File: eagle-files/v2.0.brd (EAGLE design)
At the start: 39.4 x 83.8 mm, 37 parts, among them U2 MLX90614_

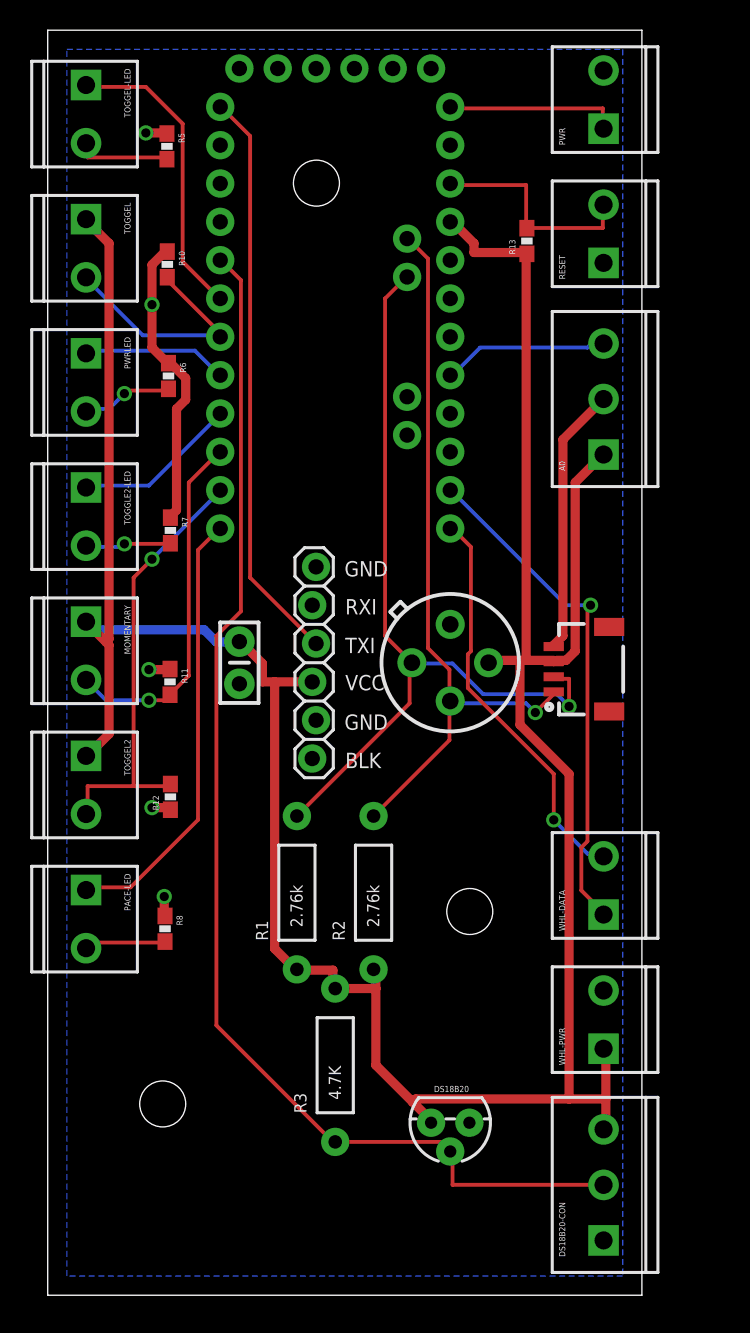
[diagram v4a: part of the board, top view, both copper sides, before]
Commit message: moved parts around on PCB for better smaller fit
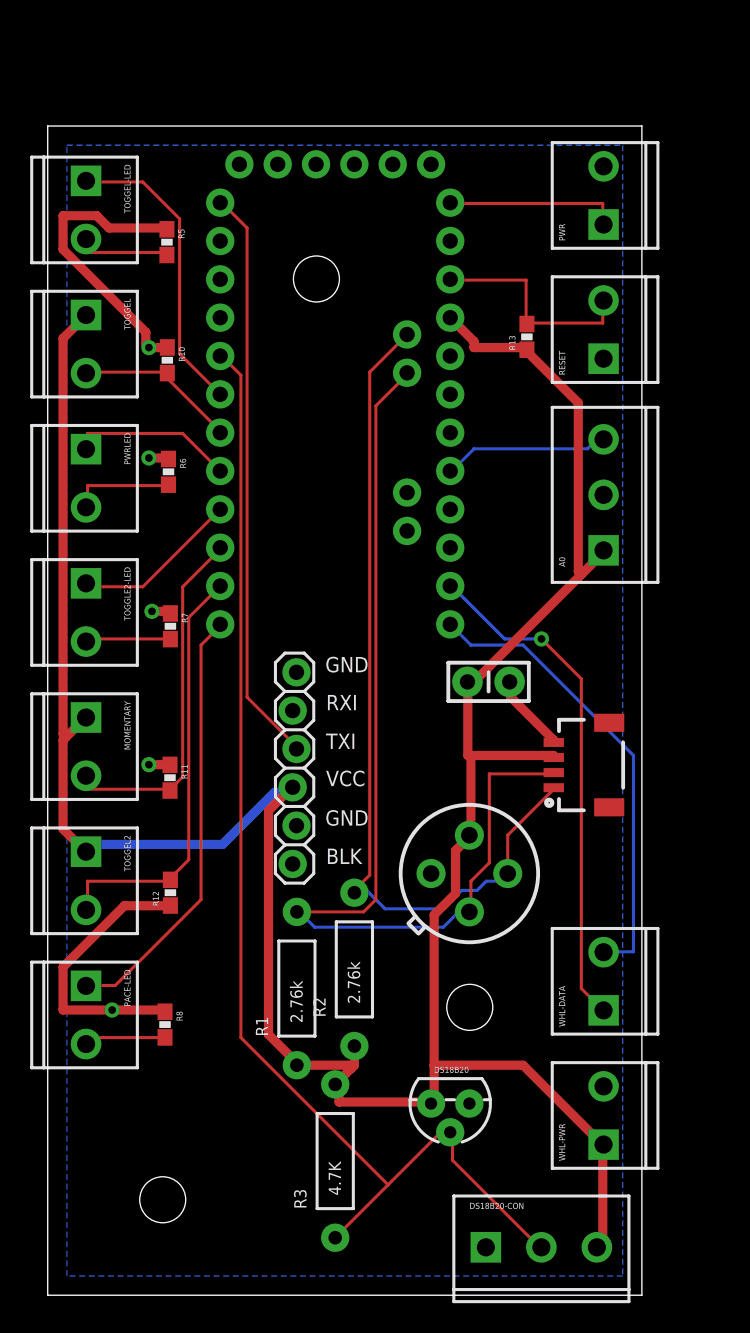
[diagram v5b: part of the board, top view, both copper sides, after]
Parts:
- moved C2 16.6 mm to (29.2, 40.6), turned to 0 degrees
- moved U2 14.0 mm to (27.9, 27.9), turned to 270 degrees
- moved DS18B20-CON 7.65 mm to (29.2, 3.17), turned to 0 degrees
- moved OPENLOG1 7.10 mm to (16.5, 41.3)
- moved PRO_MINI 6.35 mm to (19.1, 59.7)
- moved R5 6.35 mm to (7.90, 69.8)
- moved TOGGEL 6.35 mm to (2.54, 64.8)
- moved TOGGEL-LED 6.35 mm to (2.54, 73.7)
- moved A0 6.35 mm to (36.8, 49.5)
- moved JP6 6.35 mm to (28.0, 19.1)
- moved MLX1 6.35 mm to (33.5, 35.1)
- moved MOMENTARY 6.35 mm to (2.54, 38.1)
- moved PACE-LED 6.35 mm to (2.54, 20.3)
- moved R1 6.35 mm to (16.5, 20.3)
- moved R10 6.35 mm to (7.92, 62.0)
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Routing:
- net 5V: track 196.2 -> 179.2 mm
- net N$9: track 54.9 -> 67.7 mm, vias 1 -> 0
- net N$7: track 49.4 -> 57.2 mm, vias 1 -> 0
- net N$1: track 16.0 -> 10.9 mm
- net GND: track 43.0 -> 47.4 mm
- net N$11: track 26.8 -> 30.7 mm, vias 1 -> 0
- net N$2: track 83.5 -> 80.3 mm
- net N$6: track 9.67 -> 10.9 mm
- net N$18: track 29.5 -> 28.4 mm, vias 1 -> 0
- net N$14: track 6.25 -> 6.91 mm, vias 1 -> 0
- net N$17: track 29.3 -> 28.7 mm
- net N$15: track 5.74 -> 5.70 mm, vias 1 -> 0
- net N$10: vias 1 -> 0
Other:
- board size 39.4 x 83.8 mm -> 39.4 x 77.5 mm

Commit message: added base code for Arduino
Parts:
- renumbered PACE-LED to MOMENTARY-LED
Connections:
- removed net N$7: MLX1.1, PRO_MINI.A5, R2.P$2, U2.2
- removed net N$9: MLX1.2, PRO_MINI.A4, R1.P$2, U2.1
- new net N$21: MLX1.2, PRO_MINI.A5, R2.P$2, U2.2
- new net N$22: MLX1.1, PRO_MINI.A4, R1.P$2, U2.1
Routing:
- net N$9: track 67.7 -> 0.00 mm
- net N$22: track 0.00 -> 65.3 mm
- net N$21: track 0.00 -> 60.0 mm
- net N$7: track 57.2 -> 0.00 mm
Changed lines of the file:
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@@
 <element name="WHL-PWR" library="SparkFun-Connectors" package="SCREWTERMINAL-3.5MM-2_LOCK" value="" x="36.83" y="10.16" rot="R90"/>
 <element name="WHL-DATA" library="SparkFun-Connectors" package="SCREWTERMINAL-3.5MM-2_LOCK" value="" x="36.83" y="19.05" rot="R90"/>
-<element name="PACE-LED" library="SparkFun-Connectors" package="SCREWTERMINAL-3.5MM-2_LOCK" value="" x="2.54" y="20.32" rot="R270"/>
+<element name="MOMENTARY-LED" library="SparkFun-Connectors" package="SCREWTERMINAL-3.5MM-2_LOCK" value="" x="2.54" y="20.32" rot="R270"/>
 <element name="R8" library="SparkFun-Resistors" package="0603-RES" value="330" x="7.7724" y="17.9324" rot="R270">
 <attribute name="PROD_ID" value="RES-00818" x="7.7724" y="17.9324" size="1.778" layer="27" rot="R270" display="off"/>
@@
 <via x="6.7056" y="62.7888" extent="1-16" drill="0.508"/>
 <via x="4.2672" y="18.8976" extent="1-16" drill="0.508"/>
-<wire x1="36.83" y1="53.03" x2="36.83" y2="62.0522" width="0" layer="19" extent="1-1"/>
+<wire x1="36.83" y1="62.0522" x2="36.83" y2="53.03" width="0" layer="19" extent="1-1"/>
 </signal>
 <signal name="N$4">
@@
 <wire x1="16.4592" y1="36.3728" x2="16.4846" y2="36.195" width="0.2032" layer="1"/>
 <wire x1="11.5824" y1="72.3392" x2="11.43" y2="72.39" width="0.2032" layer="1"/>
-</signal>
-<signal name="N$7">
-<contactref element="MLX1" pad="1"/>
-<contactref element="U2" pad="2"/>
-<contactref element="PRO_MINI" pad="A5"/>
-<contactref element="R2" pad="P$2"/>
-<wire x1="30.48" y1="30.48" x2="33.528" y2="33.528" width="0.2032" layer="1"/>
-<wire x1="30.48" y1="27.94" x2="30.48" y2="30.48" width="0.2032" layer="1"/>
-<wire x1="33.528" y1="33.528" x2="33.528" y2="33.6282" width="0.2032" layer="1"/>
-<wire x1="21.336" y1="27.8384" x2="20.32" y2="26.8224" width="0.2032" layer="1"/>
-<wire x1="21.336" y1="61.1632" x2="21.336" y2="27.8384" width="0.2032" layer="1"/>
-<wire x1="23.7744" y1="63.6016" x2="21.336" y2="61.1632" width="0.2032" layer="1"/>
-<wire x1="20.32" y1="26.8224" x2="20.32" y2="26.67" width="0.2032" layer="1"/>
-<wire x1="23.7744" y1="63.6016" x2="23.8125" y2="63.65875" width="0.2032" layer="1"/>
-<wire x1="30.0736" y1="27.432" x2="30.48" y2="27.8384" width="0.2032" layer="16"/>
-<wire x1="29.0576" y1="27.432" x2="30.0736" y2="27.432" width="0.2032" layer="16"/>
-<wire x1="28.448" y1="26.8224" x2="29.0576" y2="27.432" width="0.2032" layer="16"/>
-<wire x1="27.432" y1="26.8224" x2="28.448" y2="26.8224" width="0.2032" layer="16"/>
-<wire x1="26.2128" y1="25.6032" x2="27.432" y2="26.8224" width="0.2032" layer="16"/>
-<wire x1="22.352" y1="25.6032" x2="26.2128" y2="25.6032" width="0.2032" layer="16"/>
-<wire x1="21.1328" y1="26.8224" x2="22.352" y2="25.6032" width="0.2032" layer="16"/>
-<wire x1="20.32" y1="26.8224" x2="21.1328" y2="26.8224" width="0.2032" layer="16"/>
-<wire x1="30.48" y1="27.8384" x2="30.48" y2="27.94" width="0.2032" layer="16"/>
-<wire x1="20.32" y1="26.8224" x2="20.32" y2="26.67" width="0.2032" layer="16"/>
-</signal>
-<signal name="N$9">
-<contactref element="MLX1" pad="2"/>
-<contactref element="U2" pad="1"/>
-<contactref element="PRO_MINI" pad="A4"/>
-<contactref element="R1" pad="P$2"/>
-<wire x1="29.2608" y1="34.544" x2="33.528" y2="34.544" width="0.2032" layer="1"/>
-<wire x1="29.2608" y1="28.6512" x2="29.2608" y2="34.544" width="0.2032" layer="1"/>
-<wire x1="28.0416" y1="27.432" x2="29.2608" y2="28.6512" width="0.2032" layer="1"/>
-<wire x1="28.0416" y1="25.4" x2="28.0416" y2="27.432" width="0.2032" layer="1"/>
-<wire x1="33.528" y1="34.544" x2="33.528" y2="34.6282" width="0.2032" layer="1"/>
-<wire x1="28.0416" y1="25.4" x2="27.94" y2="25.4" width="0.2032" layer="1"/>
-<wire x1="17.6784" y1="24.384" x2="16.6624" y2="25.4" width="0.2032" layer="16"/>
-<wire x1="26.2128" y1="24.384" x2="17.6784" y2="24.384" width="0.2032" layer="16"/>
-<wire x1="27.2288" y1="25.4" x2="26.2128" y2="24.384" width="0.2032" layer="16"/>
-<wire x1="27.94" y1="25.4" x2="27.2288" y2="25.4" width="0.2032" layer="16"/>
-<wire x1="16.6624" y1="25.4" x2="16.51" y2="25.4" width="0.2032" layer="16"/>
-<wire x1="21.7424" y1="58.928" x2="23.7744" y2="60.96" width="0.2032" layer="1"/>
-<wire x1="21.7424" y1="26.2128" x2="21.7424" y2="58.928" width="0.2032" layer="1"/>
-<wire x1="20.9296" y1="25.4" x2="21.7424" y2="26.2128" width="0.2032" layer="1"/>
-<wire x1="16.51" y1="25.4" x2="20.9296" y2="25.4" width="0.2032" layer="1"/>
-<wire x1="23.7744" y1="60.96" x2="23.8125" y2="61.11875" width="0.2032" layer="1"/>
 </signal>
 <signal name="5V" class="1">
@@
 </signal>
 <signal name="N$16">
-<contactref element="PACE-LED" pad="2"/>
+<contactref element="MOMENTARY-LED" pad="2"/>
 <contactref element="R8" pad="2"/>
 <wire x1="2.6416" y1="17.0688" x2="7.7216" y2="17.0688" width="0.2032" layer="1"/>
@@
 </signal>
 <signal name="N$17">
-<contactref element="PACE-LED" pad="1"/>
+<contactref element="MOMENTARY-LED" pad="1"/>
 <contactref element="PRO_MINI" pad="12"/>
 <wire x1="10.16" y1="43.0784" x2="11.3792" y2="44.2976" width="0.2032" layer="1"/>
@@
 <wire x1="36.7792" y1="56.6928" x2="36.83" y2="56.7078" width="0.2032" layer="16"/>
 </signal>
+<signal name="N$21">
+<contactref element="MLX1" pad="2"/>
+<contactref element="U2" pad="2"/>
+<contactref element="PRO_MINI" pad="A5"/>
+<contactref element="R2" pad="P$2"/>
+<wire x1="30.48" y1="34.544" x2="33.528" y2="34.544" width="0.2032" layer="1"/>
+<wire x1="30.48" y1="27.94" x2="30.48" y2="34.544" width="0.2032" layer="1"/>
+<wire x1="33.528" y1="34.544" x2="33.528" y2="34.6282" width="0.2032" layer="1"/>
+<wire x1="21.336" y1="27.8384" x2="20.32" y2="26.8224" width="0.2032" layer="1"/>
+<wire x1="21.336" y1="61.1632" x2="21.336" y2="27.8384" width="0.2032" layer="1"/>
+<wire x1="23.7744" y1="63.6016" x2="21.336" y2="61.1632" width="0.2032" layer="1"/>
+<wire x1="20.32" y1="26.8224" x2="20.32" y2="26.67" width="0.2032" layer="1"/>
+<wire x1="23.7744" y1="63.6016" x2="23.8125" y2="63.65875" width="0.2032" layer="1"/>
+<wire x1="30.0736" y1="27.432" x2="30.48" y2="27.8384" width="0.2032" layer="16"/>
+<wire x1="29.0576" y1="27.432" x2="30.0736" y2="27.432" width="0.2032" layer="16"/>
+<wire x1="28.448" y1="26.8224" x2="29.0576" y2="27.432" width="0.2032" layer="16"/>
+<wire x1="27.432" y1="26.8224" x2="28.448" y2="26.8224" width="0.2032" layer="16"/>
+<wire x1="26.2128" y1="25.6032" x2="27.432" y2="26.8224" width="0.2032" layer="16"/>
+<wire x1="22.352" y1="25.6032" x2="26.2128" y2="25.6032" width="0.2032" layer="16"/>
+<wire x1="21.1328" y1="26.8224" x2="22.352" y2="25.6032" width="0.2032" layer="16"/>
+<wire x1="20.32" y1="26.8224" x2="21.1328" y2="26.8224" width="0.2032" layer="16"/>
+<wire x1="30.48" y1="27.8384" x2="30.48" y2="27.94" width="0.2032" layer="16"/>
+<wire x1="20.32" y1="26.8224" x2="20.32" y2="26.67" width="0.2032" layer="16"/>
+</signal>
+<signal name="N$22">
+<contactref element="MLX1" pad="1"/>
+<contactref element="U2" pad="1"/>
+<contactref element="PRO_MINI" pad="A4"/>
+<contactref element="R1" pad="P$2"/>
+<wire x1="31.9024" y1="31.9024" x2="33.528" y2="33.528" width="0.2032" layer="1"/>
+<wire x1="31.9024" y1="27.432" x2="31.9024" y2="31.9024" width="0.2032" layer="1"/>
+<wire x1="29.8704" y1="25.4" x2="31.9024" y2="27.432" width="0.2032" layer="1"/>
+<wire x1="27.94" y1="25.4" x2="29.8704" y2="25.4" width="0.2032" layer="1"/>
+<wire x1="33.528" y1="33.528" x2="33.528" y2="33.6282" width="0.2032" layer="1"/>
+<wire x1="17.6784" y1="24.384" x2="16.6624" y2="25.4" width="0.2032" layer="16"/>
+<wire x1="26.2128" y1="24.384" x2="17.6784" y2="24.384" width="0.2032" layer="16"/>
+<wire x1="27.2288" y1="25.4" x2="26.2128" y2="24.384" width="0.2032" layer="16"/>
+<wire x1="27.94" y1="25.4" x2="27.2288" y2="25.4" width="0.2032" layer="16"/>
+<wire x1="16.6624" y1="25.4" x2="16.51" y2="25.4" width="0.2032" layer="16"/>
+<wire x1="21.7424" y1="58.928" x2="23.7744" y2="60.96" width="0.2032" layer="1"/>
+<wire x1="21.7424" y1="26.2128" x2="21.7424" y2="58.928" width="0.2032" layer="1"/>
+<wire x1="20.9296" y1="25.4" x2="21.7424" y2="26.2128" width="0.2032" layer="1"/>
+<wire x1="16.51" y1="25.4" x2="20.9296" y2="25.4" width="0.2032" layer="1"/>
+<wire x1="23.7744" y1="60.96" x2="23.8125" y2="61.11875" width="0.2032" layer="1"/>
+</signal>
 </signals>

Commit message: updated txo rxi for eagle
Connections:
- net N$8: now also OPENLOG1.2; no longer OPENLOG1.3
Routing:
- net N$8: track 38.3 -> 35.7 mm
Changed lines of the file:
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@@
 </signal>
 <signal name="N$8">
-<contactref element="OPENLOG1" pad="3"/>
 <contactref element="PRO_MINI" pad="1"/>
-<wire x1="13.208" y1="39.624" x2="16.4592" y2="36.3728" width="0.2032" layer="1"/>
-<wire x1="13.208" y1="70.7136" x2="13.208" y2="39.624" width="0.2032" layer="1"/>
+<contactref element="OPENLOG1" pad="2"/>
+<wire x1="13.208" y1="41.656" x2="16.0528" y2="38.8112" width="0.2032" layer="1"/>
+<wire x1="13.208" y1="70.7136" x2="13.208" y2="41.656" width="0.2032" layer="1"/>
 <wire x1="11.5824" y1="72.3392" x2="13.208" y2="70.7136" width="0.2032" layer="1"/>
-<wire x1="16.4592" y1="36.3728" x2="16.4846" y2="36.195" width="0.2032" layer="1"/>
+<wire x1="16.0528" y1="38.8112" x2="16.2306" y2="38.735" width="0.2032" layer="1"/>
 <wire x1="11.5824" y1="72.3392" x2="11.43" y2="72.39" width="0.2032" layer="1"/>
 </signal>

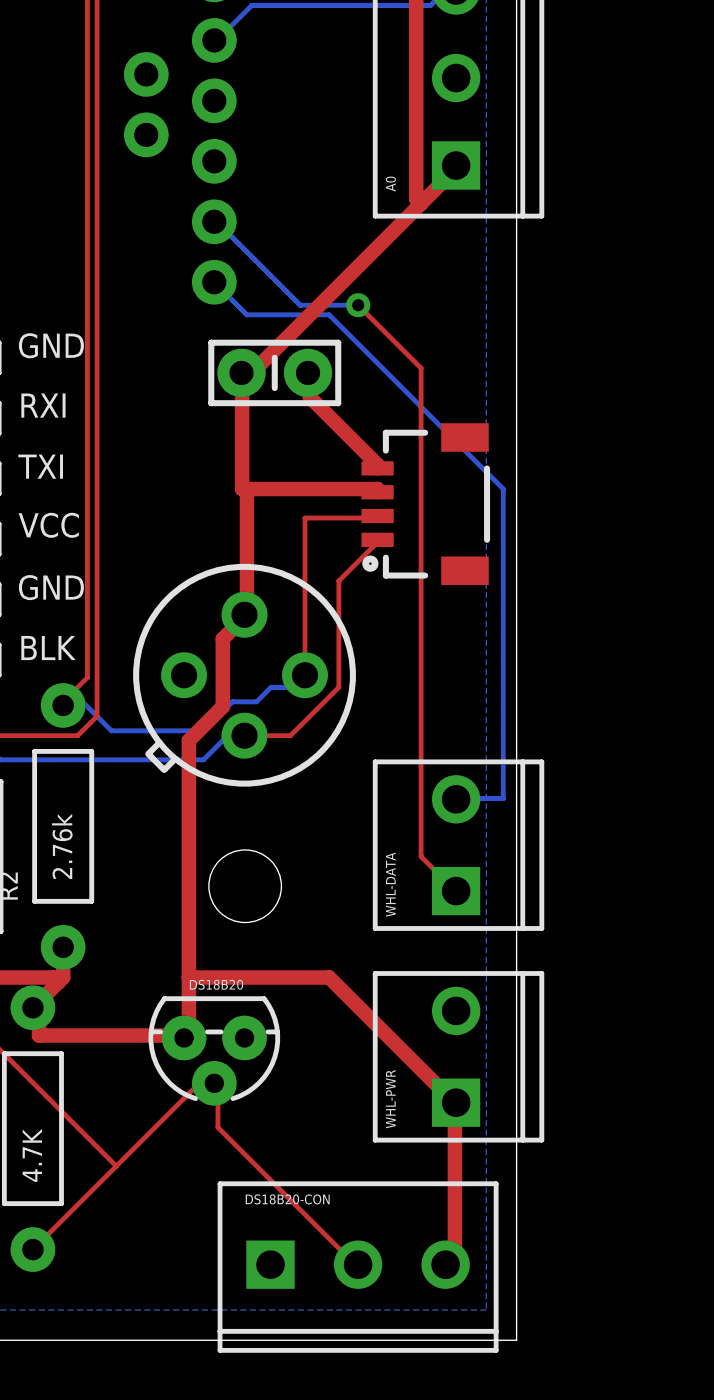
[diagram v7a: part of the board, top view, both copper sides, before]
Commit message: updated and named my analog to tmp36
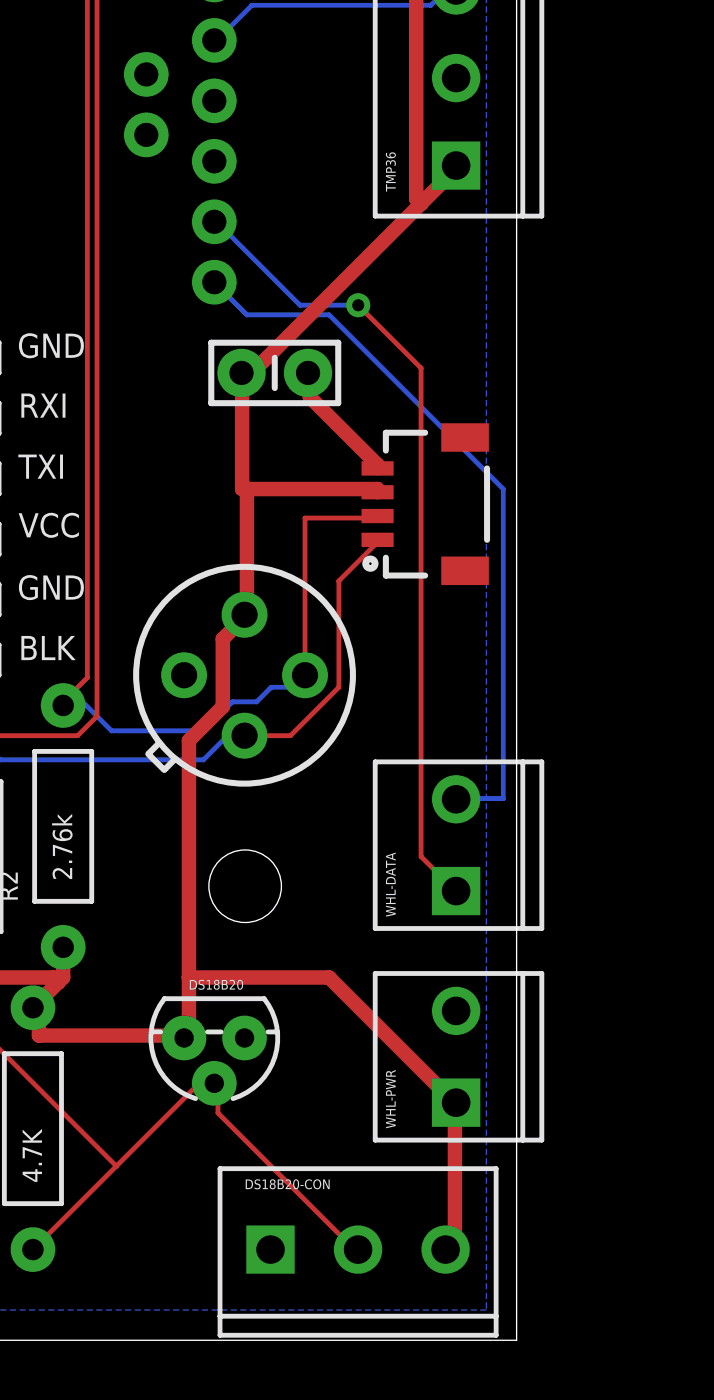
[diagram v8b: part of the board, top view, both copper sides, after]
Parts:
- moved DS18B20-CON 0.64 mm to (29.2, 3.81)
- renumbered A0 to TMP36
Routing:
- net 5V: track 179.2 -> 178.6 mm
- net N$2: track 80.3 -> 79.7 mm
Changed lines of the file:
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@@
 <attribute name="PROD_ID" value="RES-00818" x="7.7724" y="17.9324" size="1.778" layer="27" rot="R270" display="off"/>
 </element>
-<element name="DS18B20-CON" library="SparkFun-Connectors" package="SCREWTERMINAL-3.5MM-3_LOCK.007S" value="CON" x="29.21" y="3.175"/>
+<element name="DS18B20-CON" library="SparkFun-Connectors" package="SCREWTERMINAL-3.5MM-3_LOCK.007S" value="CON" x="29.21" y="3.81"/>
 <element name="RESET" library="SparkFun-Connectors" package="SCREWTERMINAL-3.5MM-2_LOCK" value="" x="36.83" y="62.23" rot="R90"/>
 <element name="R13" library="SparkFun-Resistors" package="0603-RES" value="10K" x="31.75" y="63.5" rot="R90">
 <attribute name="PROD_ID" value="RES-00824" x="31.75" y="63.5" size="1.778" layer="27" rot="R90" display="off"/>
 </element>
-<element name="A0" library="SparkFun-Connectors" package="SCREWTERMINAL-3.5MM-3_LOCK.007S" value="" x="36.83" y="49.53" rot="R90"/>
+<element name="TMP36" library="SparkFun-Connectors" package="SCREWTERMINAL-3.5MM-3_LOCK.007S" value="" x="36.83" y="49.53" rot="R90"/>
 </elements>
 <signals>
@@
 <contactref element="DS18B20-CON" pad="1"/>
 <contactref element="RESET" pad="1"/>
-<contactref element="A0" pad="2"/>
+<contactref element="TMP36" pad="2"/>
 <polygon width="0.6096" layer="16" isolate="0.3048">
 <vertex x="1.27" y="76.2"/>
@@
 <contactref element="DS18B20-CON" pad="3"/>
 <contactref element="R13" pad="1"/>
-<contactref element="A0" pad="1"/>
+<contactref element="TMP36" pad="1"/>
 <wire x1="28.2448" y1="62.7888" x2="31.6992" y2="62.7888" width="0.6096" layer="1"/>
 <wire x1="28.2448" y1="63.1952" x2="28.2448" y2="62.7888" width="0.6096" layer="1"/>
@@
 <wire x1="2.4384" y1="64.8208" x2="2.54" y2="64.9478" width="0.6096" layer="1"/>
 <wire x1="1.016" y1="37.1856" x2="1.2192" y2="36.9824" width="0.6096" layer="1"/>
-<wire x1="36.7792" y1="3.4544" x2="36.576" y2="3.2512" width="0.6096" layer="1"/>
-<wire x1="36.7792" y1="9.9568" x2="36.7792" y2="3.4544" width="0.6096" layer="1"/>
-<wire x1="36.576" y1="3.2512" x2="36.3878" y2="3.175" width="0.6096" layer="1"/>
+<wire x1="36.7792" y1="4.064" x2="36.576" y2="3.8608" width="0.6096" layer="1"/>
+<wire x1="36.7792" y1="9.9568" x2="36.7792" y2="4.064" width="0.6096" layer="1"/>
+<wire x1="36.576" y1="3.8608" x2="36.3878" y2="3.81" width="0.6096" layer="1"/>
 <wire x1="36.7792" y1="9.9568" x2="36.83" y2="9.9822" width="0.6096" layer="1"/>
 <wire x1="20.32" y1="15.24" x2="20.1168" y2="15.0368" width="0.6096" layer="1"/>
@@
 <wire x1="22.5552" y1="7.3152" x2="12.8016" y2="17.0688" width="0.2032" layer="1"/>
 <wire x1="11.5824" y1="62.1792" x2="11.43" y2="62.23" width="0.2032" layer="1"/>
-<wire x1="26.8224" y1="8.9408" x2="32.512" y2="3.2512" width="0.2032" layer="1"/>
-<wire x1="26.8224" y1="10.7696" x2="26.8224" y2="8.9408" width="0.2032" layer="1"/>
-<wire x1="32.512" y1="3.2512" x2="32.71" y2="3.175" width="0.2032" layer="1"/>
+<wire x1="26.8224" y1="9.5504" x2="32.512" y2="3.8608" width="0.2032" layer="1"/>
+<wire x1="26.8224" y1="10.7696" x2="26.8224" y2="9.5504" width="0.2032" layer="1"/>
+<wire x1="32.512" y1="3.8608" x2="32.71" y2="3.81" width="0.2032" layer="1"/>
 <wire x1="26.8224" y1="10.7696" x2="26.67" y2="10.795" width="0.2032" layer="1"/>
 </signal>
@@
 </signal>
 <signal name="N$20">
-<contactref element="A0" pad="3"/>
+<contactref element="TMP36" pad="3"/>
 <contactref element="PRO_MINI" pad="17"/>
 <wire x1="28.2448" y1="56.0832" x2="26.8224" y2="54.6608" width="0.2032" layer="16"/>
